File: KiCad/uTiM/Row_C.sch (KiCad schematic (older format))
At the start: 10 parts, among them U301 APA102, U302 APA102, U303 APA102, U304 APA102, U305 APA102, U306 APA102, U307 APA102, U308 APA102

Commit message: microTiM aka uTiM work in progress
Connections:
- net CO_C renamed CI_D
- net DO_C renamed DI_D
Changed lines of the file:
@@
 DI_C
 Text HLabel 950  3100 0    60   Output ~ 12
-CO_C
+CI_D
 Text HLabel 950  2350 0    60   Input ~ 12
 GND
@@
 5V
 Text Label 1075 3100 0    60   ~ 0
-CO_C
+CI_D
 $Comp
 L C2 C301
@@
 	10950 3350 950  3350
 Text HLabel 950  3350 0    60   Output ~ 12
-DO_C
+DI_D
 Text HLabel 950  1400 0    60   Input ~ 12
 DI_C
@@
 	1300 1600 950  1600
 Text Label 1075 3350 0    60   ~ 0
-DO_C
+DI_D
 Text Label 1075 1600 0    60   ~ 0
 CI_C

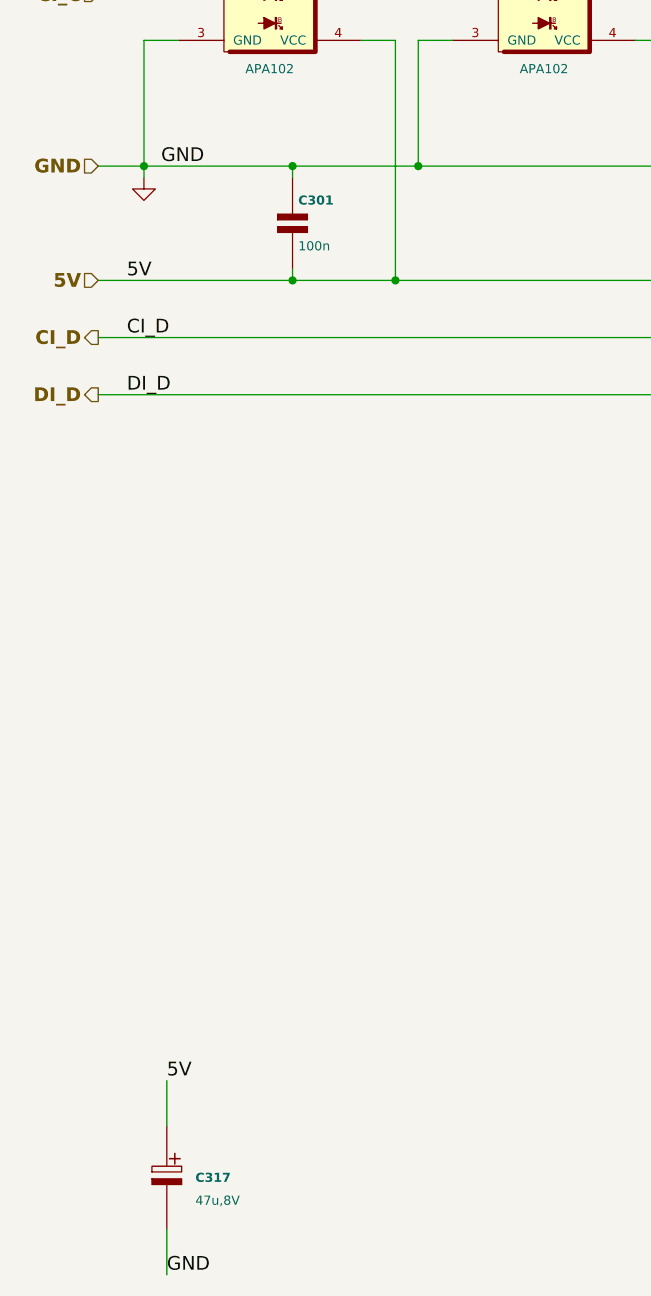
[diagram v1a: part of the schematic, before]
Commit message: work in progress, microTIM using APA102
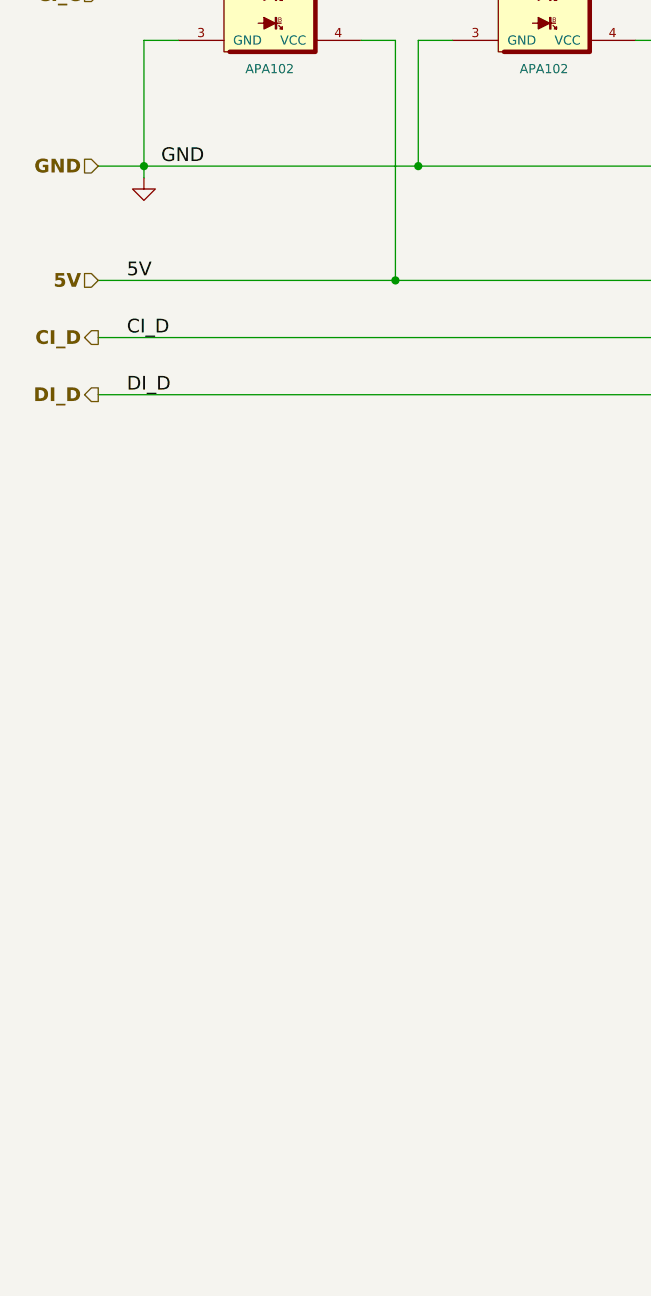
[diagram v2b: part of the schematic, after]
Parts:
- removed C301: 100n, TinyTiM_Libs:c_0805, symbol C2
- removed C317: 47u,8V, TinyTiM_Libs:c_2917, symbol C_POL_1
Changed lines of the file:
@@
 Comment4 ""
 $EndDescr
-Text Label 1250 6350 0    60   ~ 0
-5V
-Text Label 1250 7200 0    60   ~ 0
-GND
-$Comp
-L C_POL_1 C317
-U 1 1 5118AB5D
-P 1250 6750
-F 0 "C317" H 1375 6725 40  0000 L CNB
-F 1 "47u,8V" H 1375 6625 40  0000 L CNN
-F 2 "TinyTiM_Libs:c_2917" H 1250 6700 50  0001 C CNN
-F 3 "" H 1250 6750 60  0001 C CNN
-F 4 "CAP ALUM 47UF 8V 20% SMD" H 1250 6950 60  0001 L CNN "Field4"
-F 5 "47u,8V" H 1250 7050 60  0001 L CNN "Field5"
-F 6 "2917 (7343 Metric)" H 1250 7150 60  0001 L CNN "Field6"
-F 7 "Panasonic Electronic Components" H 1250 7250 60  0001 L CNN "Field7"
-F 8 "EEF-CD0K470R" H 1250 7350 60  0001 L CNN "Field8"
-F 9 "Digikey" H 1250 7450 60  0001 L CNN "Field9"
-F 10 "PCE3606CT-ND" H 1250 7550 60  0001 L CNN "Field10"
-F 11 "http://www.digikey.com/product-detail/en/EEF-CD0K470R/PCE3606CT-ND/614442" H 1250 7650 60  0001 L CNN "Field11"
-	1    1250 6750
-	1    0    0    -1
-$EndComp
-Wire Wire Line
-	1250 7000 1250 7200
-Wire Wire Line
-	1250 6550 1250 6350
 Text Label 1075 1400 0    60   ~ 0
 DI_C
@@
 CI_D
 $Comp
-L C2 C301
-U 1 1 56C296B2
-P 1800 2600
-F 0 "C301" H 1825 2700 40  0000 L CNB
-F 1 "100n" H 1825 2500 40  0000 L CNN
-F 2 "TinyTiM_Libs:c_0805" H 1800 2600 50  0001 C CNN
-F 3 "" H 1800 2600 60  0001 C CNN
-F 4 "CAP CER 0.1UF 25V 10% X7R 0805" H 1800 2800 60  0001 L CNN "Field4"
-F 5 "100nF, 25V" H 1800 2900 60  0001 L CNN "Field5"
-F 6 "Surface Mount, MLCC" H 1800 3000 60  0001 L CNN "Field6"
-F 7 "Kemet" H 1800 3100 60  0001 L CNN "Field7"
-F 8 "C0805C104K3RACTU" H 1800 3200 60  0001 L CNN "Field8"
-F 9 "Digikey" H 1800 3300 60  0001 L CNN "Field9"
-F 10 "399-1168-1-ND" H 1800 3400 60  0001 L CNN "Field10"
-F 11 "http://www.digikey.com/product-detail/en/C0805C104K3RACTU/399-1168-1-ND/411443" H 1800 3500 60  0001 L CNN "Field11"
-	1    1800 2600
-	1    0    0    -1
-$EndComp
-$Comp
 L GND #PWR09
 U 1 1 56C296B9
@@
 Wire Wire Line
 	1150 1800 1150 2400
-Connection ~ 1800 2850
-Wire Wire Line
-	1800 2850 1800 2800
 Wire Wire Line
 	950  3100 10800 3100
-Connection ~ 1800 2350
 Wire Wire Line
 	950  2350 9550 2350
@@
 	10800 3100 10800 1600
 Wire Wire Line
-	1800 2350 1800 2400
-Wire Wire Line
 	950  2850 10650 2850

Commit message: layout complete. Gerbers pending
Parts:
- renumbered U301 to U17, U302 to U18, U303 to U19, U304 to U20, U305 to U21, U306 to U22, U307 to U23, U308 to U24
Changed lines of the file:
@@
 GND
 $Comp
-L APA102 U301
+L APA102 U17
 U 1 1 56C296A0
 P 1700 1600
-F 0 "U301" H 1700 1900 40  0000 C CNB
+F 0 "U17" H 1700 1900 40  0000 C CNB
 F 1 "APA102" H 1700 1275 40  0000 C CNN
 F 2 "TinyTiM_Libs:APA102" H 1600 2000 60  0001 C CNN
@@
 5V
 $Comp
-L APA102 U302
+L APA102 U18
 U 1 1 56C296CB
 P 2900 1600
-F 0 "U302" H 2900 1900 40  0000 C CNB
+F 0 "U18" H 2900 1900 40  0000 C CNB
 F 1 "APA102" H 2900 1275 40  0000 C CNN
 F 2 "TinyTiM_Libs:APA102" H 2800 2000 60  0001 C CNN
@@
 $EndComp
 $Comp
-L APA102 U303
+L APA102 U19
 U 1 1 56C296D3
 P 4100 1600
-F 0 "U303" H 4100 1900 40  0000 C CNB
+F 0 "U19" H 4100 1900 40  0000 C CNB
 F 1 "APA102" H 4100 1275 40  0000 C CNN
 F 2 "TinyTiM_Libs:APA102" H 4000 2000 60  0001 C CNN
@@
 $EndComp
 $Comp
-L APA102 U304
+L APA102 U20
 U 1 1 56C296DB
 P 5300 1600
-F 0 "U304" H 5300 1900 40  0000 C CNB
+F 0 "U20" H 5300 1900 40  0000 C CNB
 F 1 "APA102" H 5300 1275 40  0000 C CNN
 F 2 "TinyTiM_Libs:APA102" H 5200 2000 60  0001 C CNN
@@
 $EndComp
 $Comp
-L APA102 U305
+L APA102 U21
 U 1 1 56C296E3
 P 6500 1600
-F 0 "U305" H 6500 1900 40  0000 C CNB
+F 0 "U21" H 6500 1900 40  0000 C CNB
 F 1 "APA102" H 6500 1275 40  0000 C CNN
 F 2 "TinyTiM_Libs:APA102" H 6400 2000 60  0001 C CNN
@@
 $EndComp
 $Comp
-L APA102 U306
+L APA102 U22
 U 1 1 56C296EB
 P 7700 1600
-F 0 "U306" H 7700 1900 40  0000 C CNB
+F 0 "U22" H 7700 1900 40  0000 C CNB
 F 1 "APA102" H 7700 1275 40  0000 C CNN
 F 2 "TinyTiM_Libs:APA102" H 7600 2000 60  0001 C CNN
@@
 $EndComp
 $Comp
-L APA102 U307
+L APA102 U23
 U 1 1 56C296F3
 P 8900 1600
-F 0 "U307" H 8900 1900 40  0000 C CNB
+F 0 "U23" H 8900 1900 40  0000 C CNB
 F 1 "APA102" H 8900 1275 40  0000 C CNN
 F 2 "TinyTiM_Libs:APA102" H 8800 2000 60  0001 C CNN
@@
 $EndComp
 $Comp
-L APA102 U308
+L APA102 U24
 U 1 1 56C296FB
 P 10100 1600
-F 0 "U308" H 10100 1900 40  0000 C CNB
+F 0 "U24" H 10100 1900 40  0000 C CNB
 F 1 "APA102" H 10100 1275 40  0000 C CNN
 F 2 "TinyTiM_Libs:APA102" H 10000 2000 60  0001 C CNN
